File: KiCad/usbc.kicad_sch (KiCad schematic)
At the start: 27 parts, among them J26 JACK-USBE-20PINTL, U18 ZD25Q64BSIGT, U19 TPS65987DDJRSHR, U43 H5VU25U, U44 H5VU25U, U45 H5VU25U

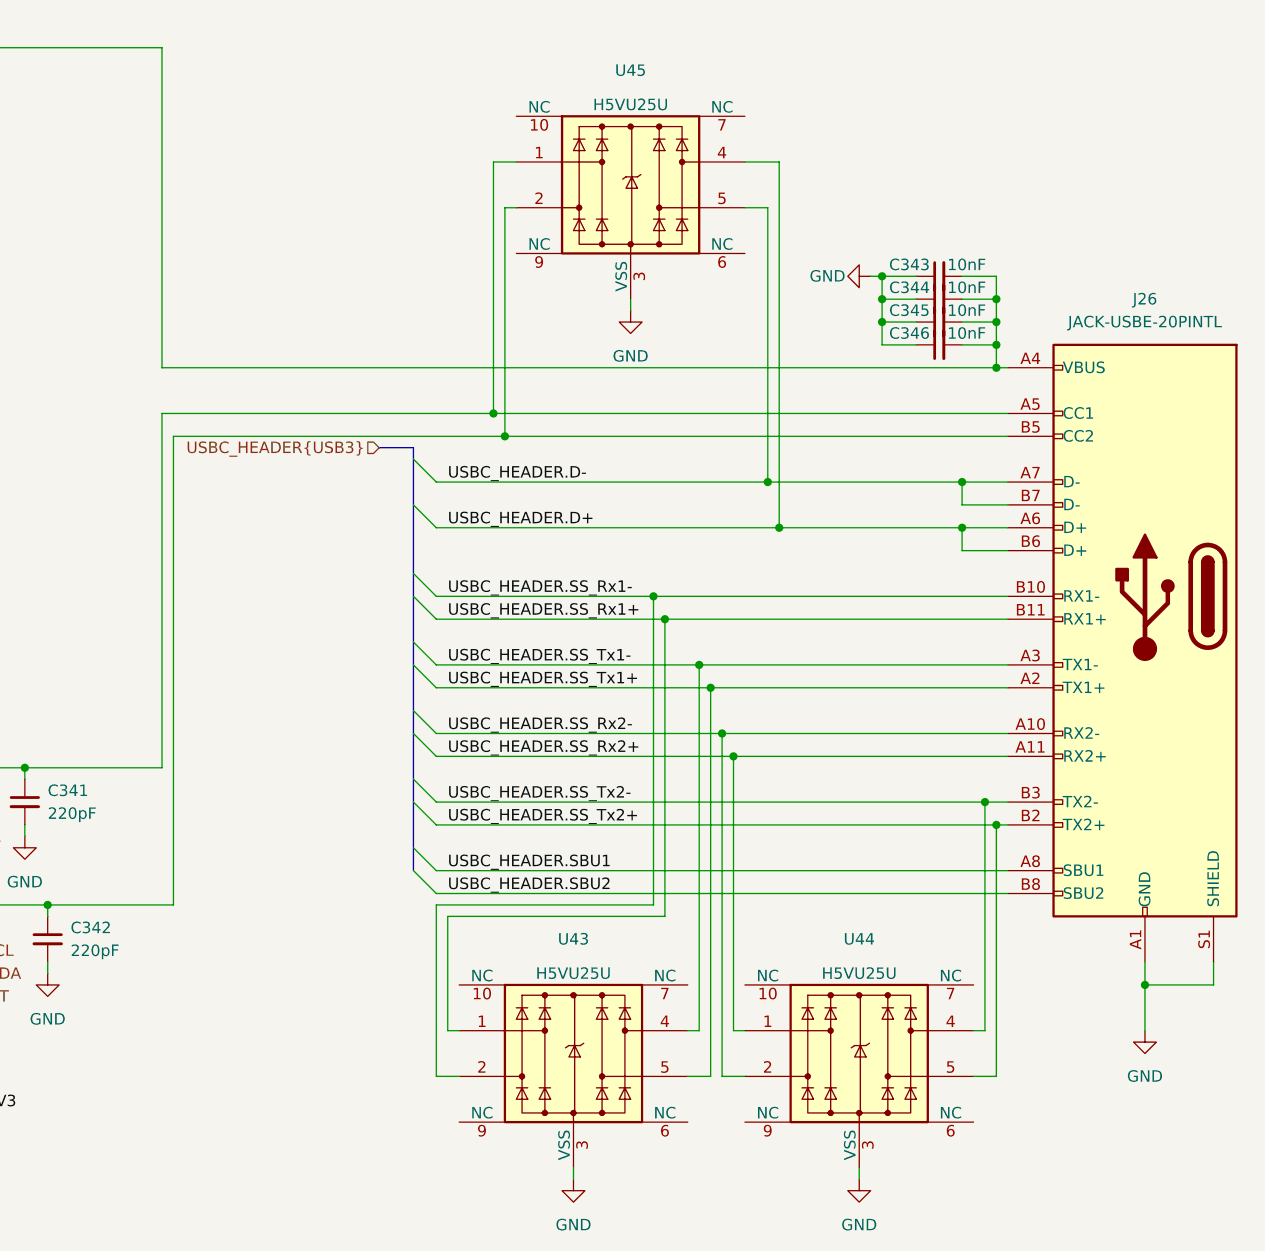
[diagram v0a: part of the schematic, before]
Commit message: Add USB Type E Header Footprint
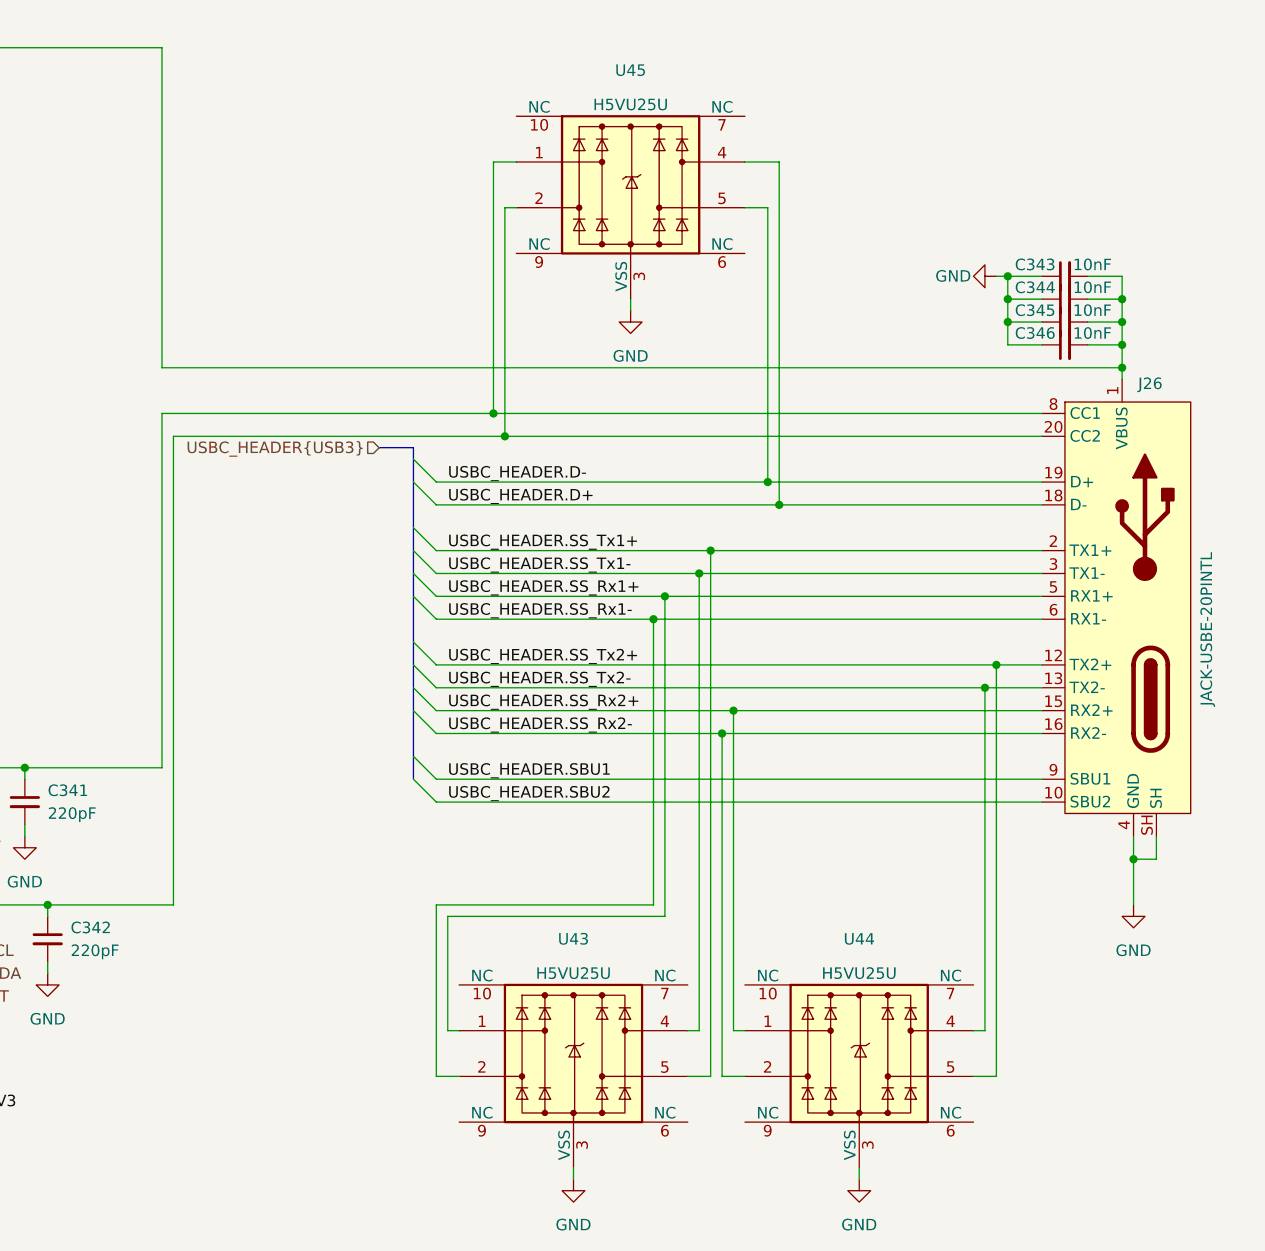
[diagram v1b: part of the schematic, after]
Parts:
- removed J26: JACK-USBE-20PINTL, symbol Connector:USB_C_Receptacle
- added J26: JACK-USBE-20PINTL, Custom:JACK-USBE-20PINTL, symbol Custom:USB_E_Header
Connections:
- net GND: now also J26.14 (GND), J26.17 (GND), J26.4 (GND), J26.SH
- net USBC_HEADER.D+: now also J26.18 (D-)
- net USBC_HEADER.D-: now also J26.19 (D+)
- net USBC_HEADER.SBU1: now also J26.9 (SBU1)
- net USBC_HEADER.SBU2: now also J26.10 (SBU2)
- net USBC_HEADER.SS_Rx1+: now also J26.5 (RX1+)
- net USBC_HEADER.SS_Rx1-: now also J26.6 (RX1-)
- net USBC_HEADER.SS_Rx2+: now also J26.15 (RX2+)
- net USBC_HEADER.SS_Rx2-: now also J26.16 (RX2-)
- net USBC_HEADER.SS_Tx1+: now also J26.2 (TX1+)
- net USBC_HEADER.SS_Tx1-: now also J26.3 (TX1-)
- net USBC_HEADER.SS_Tx2+: now also J26.12 (TX2+)
- net USBC_HEADER.SS_Tx2-: now also J26.13 (TX2-)
- net at C338.2, C339.2, C343.2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: now also J26.1 (VBUS), J26.11 (VBUS), J26.7 (VBUS)
- net at C341.1, U19.24 (C_CC1), U45.1: now also J26.8 (CC1)
- net at C342.1, U19.26 (C_CC2), U45.2: now also J26.20 (CC2)
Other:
- moved on the sheet: C343, C344, C345, C346

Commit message: Lots of tiny capacitors
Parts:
- C332: footprint (none) -> Capacitor_SMD:C_0402_1005Metric
- C333, C334, C335, C336, C337: footprint (none) -> Capacitor_SMD:C_0603_1608Metric
- U19: footprint RSH0056E-MFG -> TPS65987D:RSH0056E-MFG
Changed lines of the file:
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@@
 			)
 		)
-		(property "Footprint" ""
+		(property "Footprint" "Capacitor_SMD:C_0603_1608Metric"
 			(at 85.09 24.13 0)
 			(effects
@@
 			)
 		)
-		(property "Footprint" ""
+		(property "Footprint" "Capacitor_SMD:C_0603_1608Metric"
 			(at 97.79 27.94 0)
 			(effects
@@
 			)
 		)
-		(property "Footprint" "RSH0056E-MFG"
+		(property "Footprint" "TPS65987D:RSH0056E-MFG"
 			(at 53.34 111.76 0)
 			(effects
@@
 			)
 		)
-		(property "Footprint" ""
+		(property "Footprint" "Capacitor_SMD:C_0603_1608Metric"
 			(at 92.71 27.94 0)
 			(effects
@@
 			)
 		)
-		(property "Footprint" "RSH0056E-MFG"
+		(property "Footprint" "TPS65987D:RSH0056E-MFG"
 			(at 115.57 33.02 0)
 			(effects
@@
 			)
 		)
-		(property "Footprint" ""
+		(property "Footprint" "Capacitor_SMD:C_0603_1608Metric"
 			(at 82.55 24.13 0)
 			(effects
@@
 			)
 		)
-		(property "Footprint" ""
+		(property "Footprint" "Capacitor_SMD:C_0603_1608Metric"
 			(at 71.12 29.21 0)
 			(effects
@@
 			)
 		)
-		(property "Footprint" ""
+		(property "Footprint" "Capacitor_SMD:C_0402_1005Metric"
 			(at 29.21 149.86 0)
 			(effects

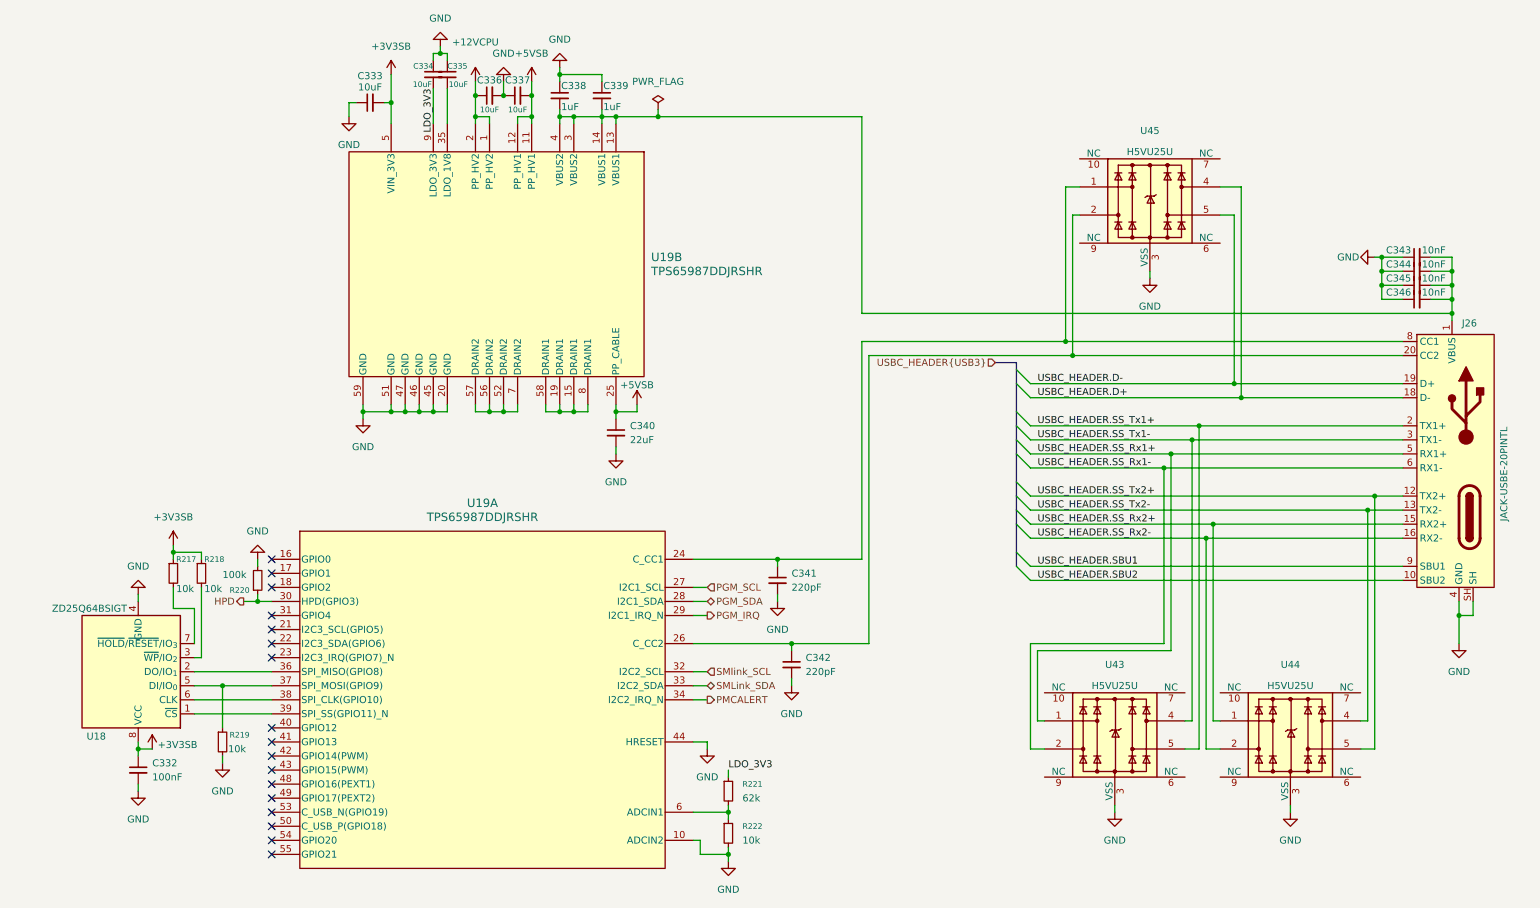
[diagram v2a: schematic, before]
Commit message: Add most passive component footprints
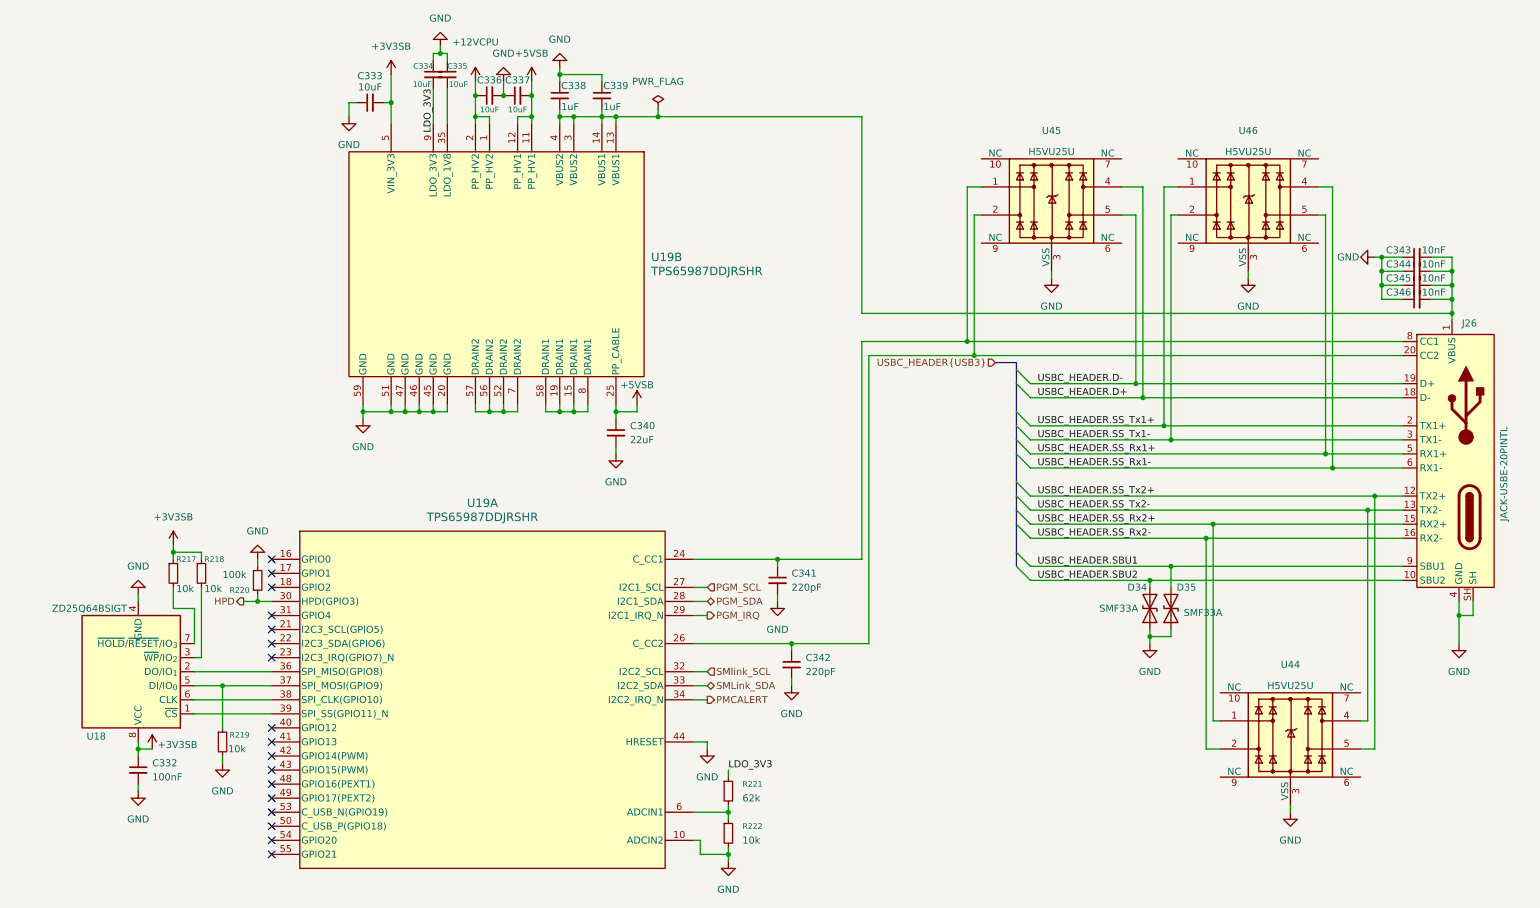
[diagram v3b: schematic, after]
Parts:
- removed U43: H5VU25U, Package_DFN_QFN:Diodes_UDFN-10_1.0x2.5mm_P0.5mm, symbol Power_Protection:D3V3XA4B10LP
- added D34, D35: SMF33A, Diode_SMD:D_SOD-123F, symbol Device:D_TVS
- added U46: H5VU25U, Package_DFN_QFN:Diodes_UDFN-10_1.0x2.5mm_P0.5mm, symbol Power_Protection:D3V3XA4B10LP
- C338, C339, C341, C342, C343, C344, C345, C346: footprint (none) -> Capacitor_SMD:C_0402_1005Metric
- C340: footprint (none) -> Capacitor_SMD:C_0603_1608Metric
- R217, R218, R219, R220, R222: footprint (none) -> Resistor_SMD:R_0402_1005Metric
- R221: footprint (none) -> Resistor_SMD:R_0603_1608Metric
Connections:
- net GND: now also D34.1 (A1), D35.1 (A1), U46.3 (VSS), U46.8 (VSS)
- net USBC_HEADER.SBU1: now also D35.2 (A2)
- net USBC_HEADER.SBU2: now also D34.2 (A2)
- net USBC_HEADER.SS_Rx1+: now also U46.5
- net USBC_HEADER.SS_Rx1-: now also U46.4
- net USBC_HEADER.SS_Tx1+: now also U46.1
- net USBC_HEADER.SS_Tx1-: now also U46.2
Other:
- moved on the sheet: U45

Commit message: Finish fixing footprints
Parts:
- renumbered C334 to C332, C335 to C333, C336 to C334, C337 to C335, C338 to C336, C339 to C337, C333 to C338, C343 to C339, C344 to C340, C345 to C341, C346 to C342, C340 to C343, C341 to C344, C342 to C345, C332 to C346, D34 to D37, D35 to D38, J26 to J27, R217 to R216, R218 to R217, R220 to R218, R221 to R220, R222 to R221, U19 to U40, U45 to U41, U46 to U42, U18 to U43

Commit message: Re-annotate schematic
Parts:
- renumbered C332 to C342, C333 to C343, C334 to C344, C335 to C345, C336 to C346, C337 to C347, C338 to C348, C339 to C349, C340 to C350, C341 to C351, C342 to C352, C343 to C353, C344 to C354, C345 to C355, C346 to C356, J27 to J25, R216 to R209, R217 to R210, R218 to R211, R219 to R212, R220 to R213, R221 to R214
